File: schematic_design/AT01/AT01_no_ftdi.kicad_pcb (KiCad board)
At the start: 2 copper layers, 70 x 55 mm, 55 parts, among them J1 JST Connector, J2 USB_C_Receptacle_USB2.0, J3 Conn_01x08, J4 Solenoid Valve Connector, J5 DC Pump Connector, Q1 DMG2301L, SW1 SW_Push, SW2 SW_Push, SW3 SW_Push, SW4 SW_Push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

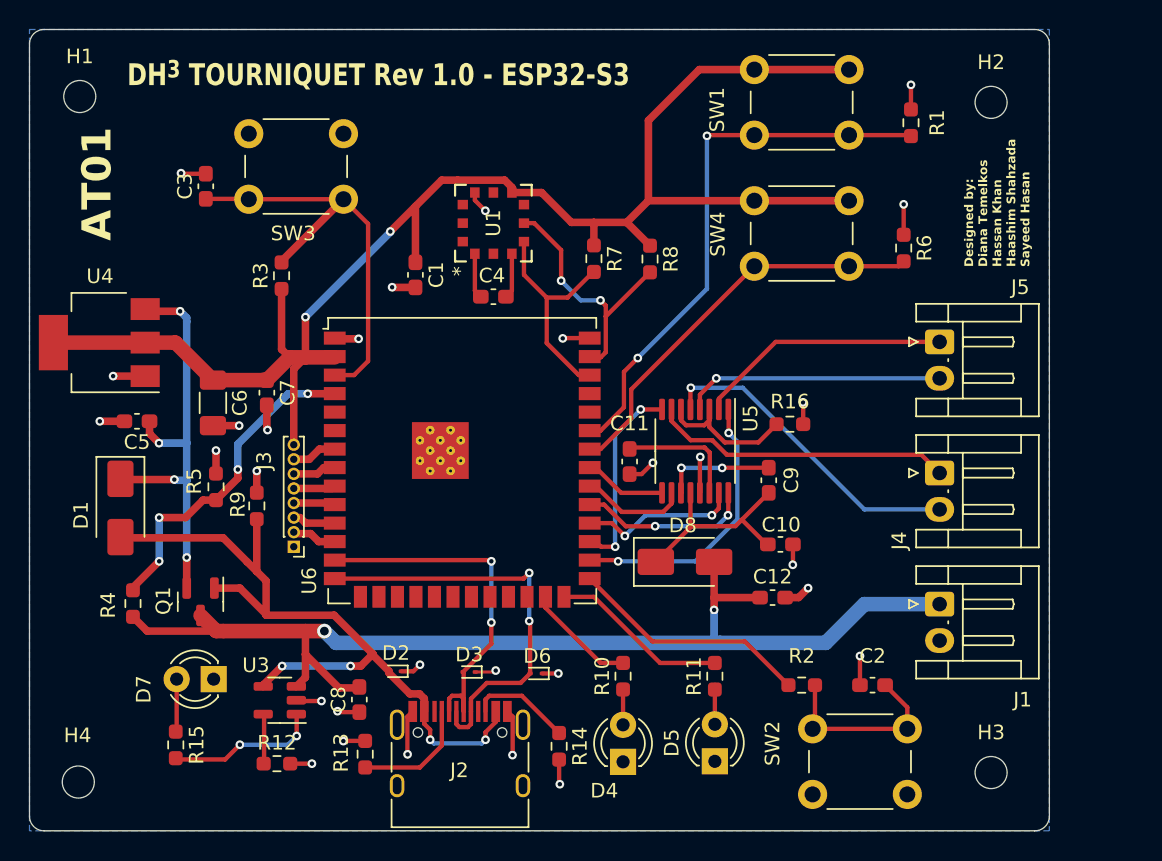
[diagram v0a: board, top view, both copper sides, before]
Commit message: added redesigned charging circuit
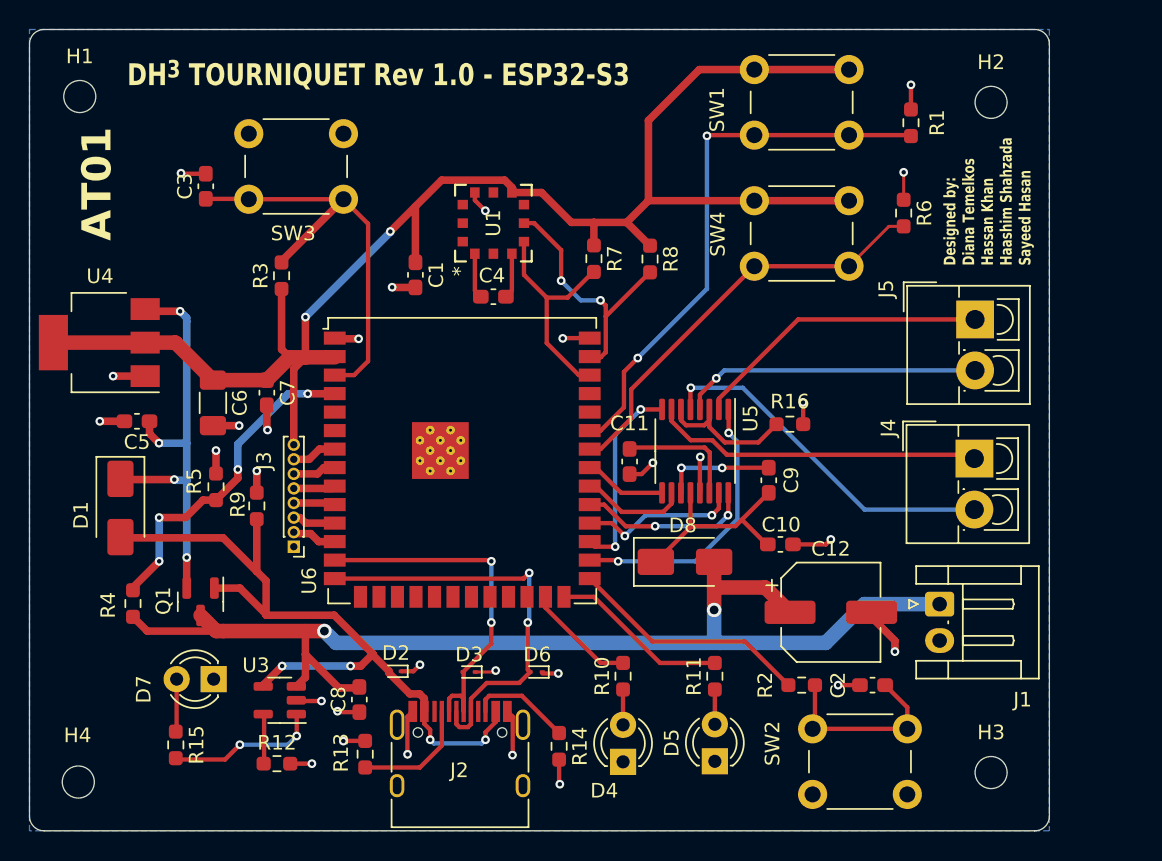
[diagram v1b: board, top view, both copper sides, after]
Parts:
- C12: footprint Capacitor_SMD:C_0603_1608Metric_Pad1.08x0.95mm_HandSolder -> Capacitor_SMD:CP_Elec_6.3x5.2
- J4, J5: footprint Connector_JST:JST_EH_S2B-EH_1x02_P2.50mm_Horizontal -> TerminalBlock_4Ucon:TerminalBlock_4Ucon_1x02_P3.50mm_Vertical
- moved C12 4.12 mm to (171.0, 110.0)
- moved J5 2.88 mm to (180.9, 89.9)
- moved J4 2.58 mm to (180.9, 99.5)
- moved R6 2.40 mm to (176.0, 82.6)
- moved D6 0.10 mm to (150.8, 114.1)
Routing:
- net Net-(J5-Pin_1): track 17.5 -> 20.6 mm
- net VBAT: track 76.7 -> 79.5 mm
- net Net-(J5-Pin_2): track 17.9 -> 20.6 mm
- net Net-(J4-Pin_2): track 22.0 -> 24.4 mm
- net GND: track 52.0 -> 54.3 mm
- net Net-(J4-Pin_1): track 20.7 -> 22.7 mm
- net Net-(U6-IO41): track 28.1 -> 29.1 mm

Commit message: PCB redesign for new charging circuit with Espressif recommendations
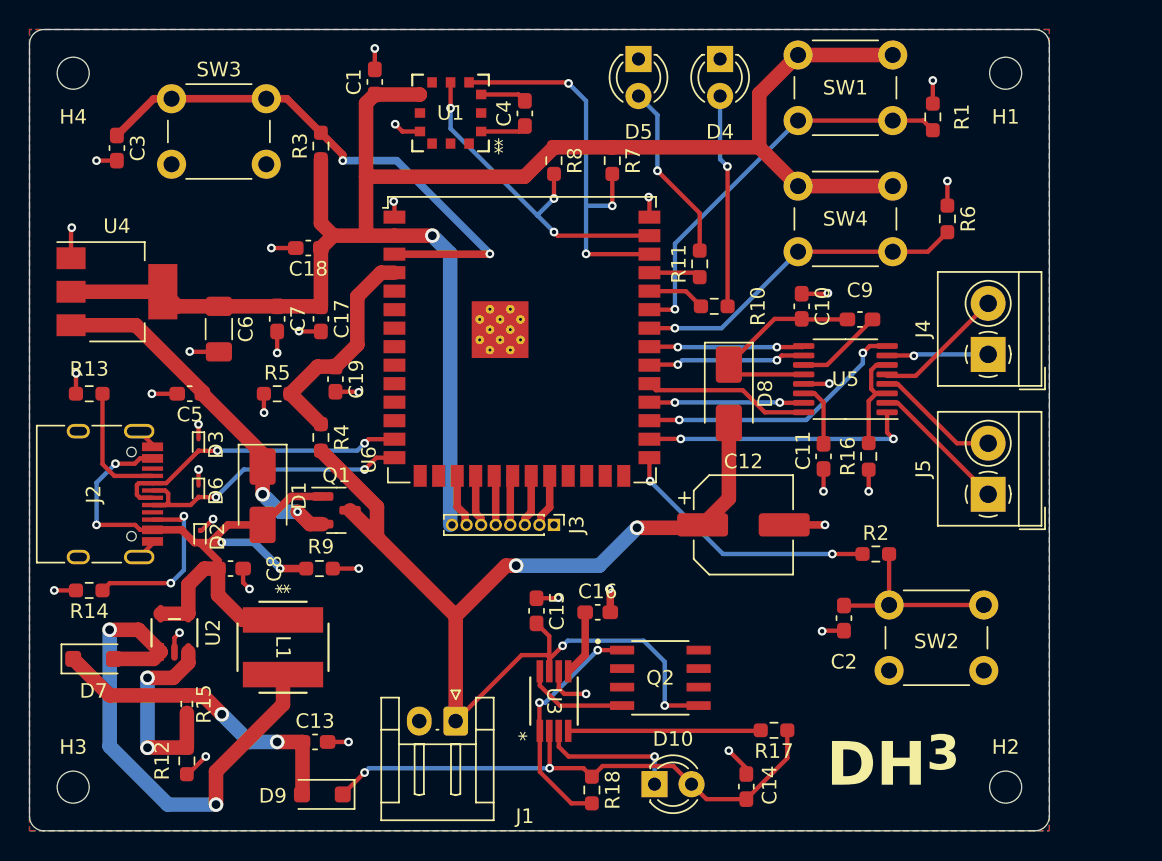
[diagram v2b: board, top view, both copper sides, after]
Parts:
- added C13: 10uF, Capacitor_SMD:C_0603_1608Metric_Pad1.08x0.95mm_HandSolder, F.Cu at (135.6, 118.9)
- added C14: 10uF, Capacitor_SMD:C_0603_1608Metric_Pad1.08x0.95mm_HandSolder, F.Cu at (165.2, 122.0)
- added C15: 10uF, Capacitor_SMD:C_0603_1608Metric_Pad1.08x0.95mm_HandSolder, F.Cu at (150.8, 109.9)
- added C16: 0.1uF, Capacitor_SMD:C_0603_1608Metric_Pad1.08x0.95mm_HandSolder, F.Cu at (155.0, 110.0)
- added C17: 22uF, Capacitor_SMD:C_0603_1608Metric_Pad1.08x0.95mm_HandSolder, F.Cu at (136.0, 89.9)
- added C18: 0.1uF, Capacitor_SMD:C_0603_1608Metric_Pad1.08x0.95mm_HandSolder, F.Cu at (135.1, 85.0)
- added C19: 1uF, Capacitor_SMD:C_0603_1608Metric_Pad1.08x0.95mm_HandSolder, F.Cu at (137.0, 94.0)
- added D10: LED, LED_THT:LED_D3.0mm, F.Cu at (158.9, 121.8)
- added D9: MBRM120LT3G, Diode_SMD:D_SOD-123F, F.Cu at (136.1, 122.5)
- added L1: 2.7uH, Library:IND_R2NC_SUM, F.Cu at (133.4, 112.4)
- added Q2: FDS6375, Library:SOIC127P600X175-8N, F.Cu at (159.3, 114.5)
- added R17: 100K, Resistor_SMD:R_0603_1608Metric_Pad0.98x0.95mm_HandSolder, F.Cu at (167.1, 118.1)
- added R18: 100m, Resistor_SMD:R_0603_1608Metric_Pad0.98x0.95mm_HandSolder, F.Cu at (154.6, 122.2)
- added U2: LT1935ES5-TRPBF, Library:S_5_ADI, F.Cu at (126.0, 111.4)
- D7: value LED -> MBRM120LT3G; footprint LED_THT:LED_D3.0mm -> Diode_SMD:D_SOD-123F
- J4, J5: footprint TerminalBlock_4Ucon:TerminalBlock_4Ucon_1x02_P3.50mm_Vertical -> TerminalBlock_4Ucon:TerminalBlock_4Ucon_1x02_P3.50mm_Horizontal
- R12: value 5.1K -> 10K
- R15: value 5.1K -> 61.2K; footprint Resistor_SMD:R_0603_1608Metric_Pad0.98x0.95mm_HandSolder -> Resistor_SMD:R_0402_1005Metric_Pad0.72x0.64mm_HandSolder
- U3: value MCP73831-2-OT -> MCP73844T-840I/MS; footprint Package_TO_SOT_SMD:SOT-23-5 -> Library:MSOP8_MC_MCH
- U6: value ESP32-WROOM-32 -> ESP32-S3-WROOM
- moved H1 63.6 mm to (183.0, 73.0)
- moved H3 63.0 mm to (119.0, 122.0)
- moved D4 48.7 mm to (163.4, 72.0), turned to -90 degrees
- moved H4 48.7 mm to (119.0, 73.0)
- moved D5 48.5 mm to (157.8, 72.0), turned to -90 degrees
- moved H2 47.0 mm to (183.0, 122.0)
- moved J1 34.2 mm to (145.2, 117.5), turned to 180 degrees
- moved R14 34.0 mm to (120.1, 108.5), turned to 180 degrees
- moved J2 31.5 mm to (120.4, 101.9), turned to -90 degrees
- moved R13 31.2 mm to (120.1, 95.0), turned to 180 degrees
- moved R11 28.3 mm to (162.0, 86.1)
- moved D6 26.3 mm to (127.6, 101.7), turned to -90 degrees
- moved R10 26.1 mm to (163.0, 89.0), turned to 180 degrees
- moved D3 24.3 mm to (127.6, 98.5), turned to -90 degrees
- moved U3 18.8 mm to (152.0, 116.1), turned to 90 degrees
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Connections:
- C8 pad 1: GND -> VBUS
- C8 pad 2: VBAT -> GND
- D7 pad 1: GND -> Net-(D7-K)
- J3 pad 4: BL_SCREEN -> SCK
- J3 pad 5: SCK -> MOSI
- J3 pad 6: MOSI -> CS
- J3 pad 7: CS -> BL_SCREEN
- R10 pad 2: Net-(U6-IO48) -> Net-(U6-RXD0)
- R11 pad 1: Net-(D5-A) -> Net-(U6-TXD0)
- R11 pad 2: Net-(U6-IO45) -> Net-(D5-A)
- R12 pad 1: Net-(U3-PROG) -> Net-(U2-FB)
- R15 pad 1: Net-(D7-A) -> Net-(D7-K)
- R15 pad 2: Net-(U3-STAT) -> Net-(U2-FB)
- U3 pad 1: Net-(U3-STAT) -> Net-(U3-SENSE)
- U3 pad 2: GND -> Net-(D10-A)
- U3 pad 3: VBAT -> Net-(D10-K)
- U3 pad 4: VBUS -> Net-(U3-EN)
- U3 pad 5: Net-(U3-PROG) -> Net-(U3-TIMER)
- U6 pad 10: BL_SCREEN -> unconnected-(U6-IO17-Pad10)
- U6 pad 11: RST_SCREEN -> unconnected-(U6-IO18-Pad11)
- U6 pad 12: DC_SCREEN -> unconnected-(U6-IO8-Pad12)
- U6 pad 17: unconnected-(U6-IO9-Pad17) -> BL_SCREEN
- U6 pad 18: unconnected-(U6-IO10-Pad18) -> CS
- U6 pad 19: unconnected-(U6-IO11-Pad19) -> MOSI
- U6 pad 20: unconnected-(U6-IO12-Pad20) -> SCK
- U6 pad 21: unconnected-(U6-IO13-Pad21) -> RST_SCREEN
- U6 pad 22: unconnected-(U6-IO14-Pad22) -> DC_SCREEN
- U6 pad 25: Net-(U6-IO48) -> unconnected-(U6-IO48-Pad25)
- U6 pad 26: Net-(U6-IO45) -> unconnected-(U6-IO45-Pad26)
- U6 pad 36: RXD0 -> Net-(U6-RXD0)
- U6 pad 37: TXD0 -> Net-(U6-TXD0)
- U6 pad 7: CS -> unconnected-(U6-IO7-Pad7)
- U6 pad 8: MOSI -> unconnected-(U6-IO15-Pad8)
- U6 pad 9: SCK -> unconnected-(U6-IO16-Pad9)
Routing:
- net Net-(D10-A): track 0.00 -> 38.4 mm, vias 0 -> 2
- net Net-(D7-A): track 3.62 -> 35.3 mm, vias 0 -> 2
- net Net-(D7-K): track 0.00 -> 21.7 mm, vias 0 -> 2
- net Net-(U3-SENSE): track 0.00 -> 16.4 mm, vias 0 -> 2
- net Net-(J4-Pin_1): track 22.7 -> 6.99 mm, vias 0 -> 1
- net Net-(J4-Pin_2): track 24.4 -> 9.09 mm, vias 1 -> 0
- net 3V3: track 106.7 -> 120.6 mm, vias 2 -> 1
- net Net-(U2-FB): track 0.00 -> 13.9 mm, vias 0 -> 2
- net Net-(U3-EN): track 0.00 -> 13.2 mm
- net Net-(U6-IO45): track 12.2 -> 0.00 mm
- net SCL: track 15.4 -> 27.4 mm, vias 0 -> 3
- net Net-(J5-Pin_2): track 20.6 -> 8.63 mm, vias 1 -> 0
- net Net-(D4-A): track 2.74 -> 14.6 mm, vias 0 -> 1
- net Net-(J5-Pin_1): track 20.6 -> 9.57 mm
- net Net-(U3-STAT): track 10.5 -> 0.00 mm, vias 2 -> 0
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- added copper zone on F.Cu, net GND
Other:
- board text added: "DH^{3}"
- board text removed: "AT01"
- board text removed: "DH^{3} TOURNIQUET Rev 1.0 - ESP32-S3"
- board text removed: "Designed by: Diana Temelkos Hassan Khan Haashim Shahzada Sayeed Hasan"
